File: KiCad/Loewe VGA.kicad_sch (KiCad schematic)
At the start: 29 parts, among them U1 74HCT86

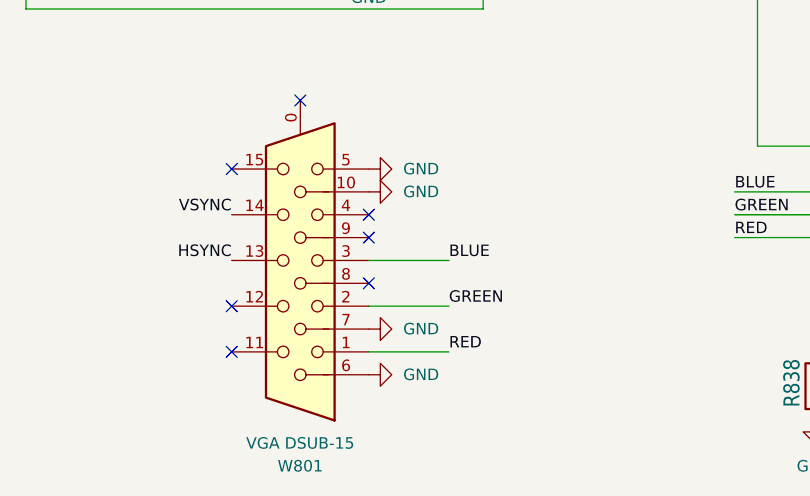
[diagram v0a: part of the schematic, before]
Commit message: Connect VGA pin 8 to GND.
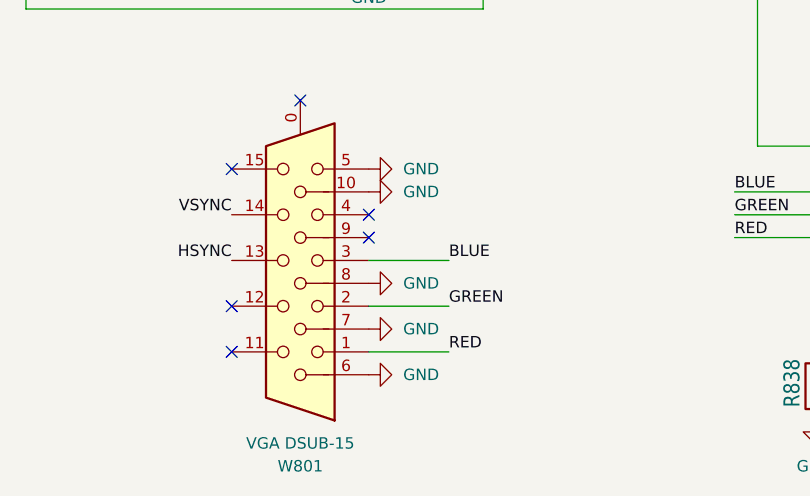
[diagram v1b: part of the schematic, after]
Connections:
- net GND: now also W801.8
- no-connect marks 7 -> 6
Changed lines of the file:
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@@
 		(at 132.08 143.51)
 	)
-	(no_connect
-		(at 132.08 151.13)
-	)
 	(wire
 		(pts
@@
 					(unit 1)
 				)
+			)
+		)
+	)
+	(symbol
+		(lib_id "power:GND")
+		(at 132.08 151.13 90)
+		(unit 1)
+		(exclude_from_sim no)
+		(in_bom yes)
+		(on_board yes)
+		(dnp no)
+		(fields_autoplaced yes)
+		(property "Reference" "#PWR013"
+			(at 138.43 151.13 0)
+			(effects
+				(font
+					(size 1.27 1.27)
+				)
+				(hide yes)
+			)
+		)
+		(property "Value" "GND"
+			(at 135.89 151.1301 90)
+			(effects
+				(font
+					(size 1.27 1.27)
+				)
+				(justify right)
+			)
+		)
+		(property "Footprint" ""
+			(at 132.08 151.13 0)
+			(effects
+				(font
+					(size 1.27 1.27)
+				)
+				(hide yes)
+			)
+		)
+		(property "Datasheet" ""
+			(at 132.08 151.13 0)
+			(effects
+				(font
+					(size 1.27 1.27)
+				)
+				(hide yes)
+			)
+		)
+		(property "Description" "Power symbol creates a global label with name \"GND\" , ground"
+			(at 132.08 151.13 0)
+			(effects
+				(font
+					(size 1.27 1.27)
+				)
+				(hide yes)
+			)
+		)
+		(pin "1"
+		)
+		(instances
+			(project "Loewe VGA"
+				(path "/a1c137e0-772e-4d1d-9f66-964ee6eebaf2"
+					(reference "#PWR013")
+					(unit 1)
+				)

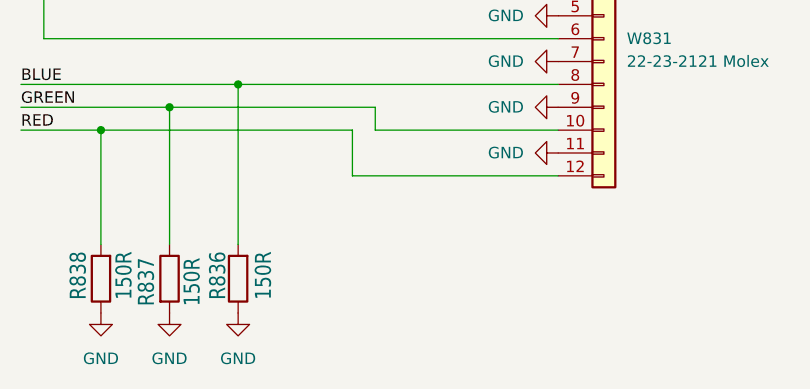
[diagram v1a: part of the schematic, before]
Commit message: Do not solder R836~R838 RGB input termination resistors for Q2400 chassis. Source: Loewe Q2400 service manual, p.2-22.
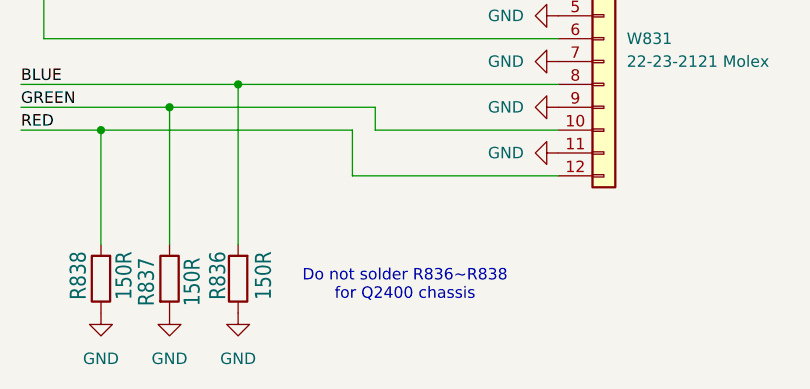
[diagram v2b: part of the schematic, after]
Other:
- note added: "Do not solder R836~R838 for Q2400 chassis"
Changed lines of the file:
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@@
+		)
+	)
+	(text "Do not solder R836~R838\nfor Q2400 chassis"
+		(exclude_from_sim no)
+		(at 215.392 163.322 0)
+		(effects
+			(font
+				(size 1.27 1.27)
+			)
 		)
 	)

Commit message: Replace custom 3225 footprint for L826, L816 with standard 1210(3225). Add 4.7uH value for L826, L816 to schematic (use value from Q2300 board).
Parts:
- L816, L826: value LL3225M -> 4u7; footprint Loewe VGA:L3225M -> Inductor_SMD:L_1210_3225Metric_Pad1.42x2.65mm_HandSolder
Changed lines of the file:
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@@
 			)
 		)
-		(property "Value" "LL3225M"
+		(property "Value" "4u7"
 			(at 88.9 52.832 90)
 			(effects
@@
 			)
 		)
-		(property "Footprint" "Loewe VGA:L3225M"
+		(property "Footprint" "Inductor_SMD:L_1210_3225Metric_Pad1.42x2.65mm_HandSolder"
 			(at 92.71 49.53 0)
 			(effects
@@
 			)
 		)
-		(property "Value" "LL3225M"
+		(property "Value" "4u7"
 			(at 83.82 90.932 90)
 			(effects
@@
 			)
 		)
-		(property "Footprint" "Loewe VGA:L3225M"
+		(property "Footprint" "Inductor_SMD:L_1210_3225Metric_Pad1.42x2.65mm_HandSolder"
 			(at 87.63 87.63 0)
 			(effects

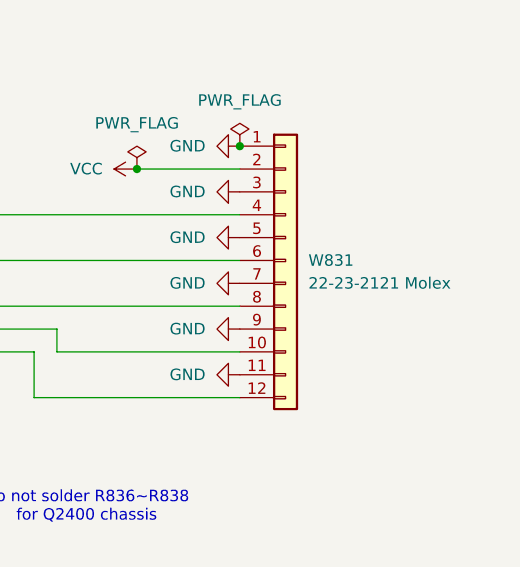
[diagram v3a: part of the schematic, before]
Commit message: Replace JST XH 2.50 mm with custom 2.54 mm. Remove unused Molex 22-23-2121 footprint. Add version V.1.1 label to PCB silkscreen.
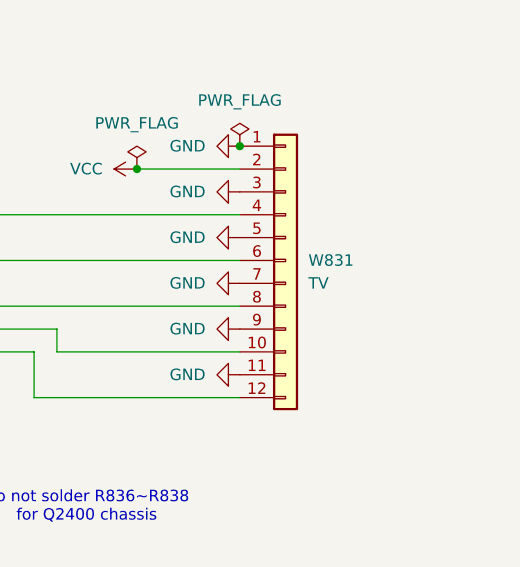
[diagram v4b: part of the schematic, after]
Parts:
- W831: value 22-23-2121 Molex -> TV; footprint Loewe VGA:22-23-2121 -> JST_XH_S10B_2.54mm:JST_XH_B12B-XH-A_1x12_P2.54mm_Vertical
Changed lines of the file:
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@@
 			)
 		)
-		(property "Value" "22-23-2121 Molex"
+		(property "Value" "TV"
 			(at 240.03 138.4299 0)
 			(effects
@@
 			)
 		)
-		(property "Footprint" "Loewe VGA:22-23-2121"
+		(property "Footprint" "JST_XH_S10B_2.54mm:JST_XH_B12B-XH-A_1x12_P2.54mm_Vertical"
 			(at 237.49 135.89 0)
 			(effects

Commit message: Replace incorrect Connector_Dsub:DSUB-15-HD_Male with short Connector_Dsub:DSUB-15-HD_Female. Move VGA and TV connectors to back side. Reduce PCB width. Change VCC tracks width from 0.3 to 0.5 mm. Align board info text.
PCB version updated to 1.2.
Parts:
- W801: footprint Connector_Dsub:DSUB-15-HD_Male_Horizontal_P2.29x1.98mm_EdgePinOffset8.35mm_Housed_MountingHolesOffset10.89mm -> Connector_Dsub:DSUB-15-HD_Female_Horizontal_P2.29x1.98mm_EdgePinOffset3.03mm_Housed_MountingHolesOffset4.94mm
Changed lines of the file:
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@@
 			)
 		)
-		(property "Footprint" "Connector_Dsub:DSUB-15-HD_Male_Horizontal_P2.29x1.98mm_EdgePinOffset8.35mm_Housed_MountingHolesOffset10.89mm"
+		(property "Footprint" "Connector_Dsub:DSUB-15-HD_Female_Horizontal_P2.29x1.98mm_EdgePinOffset3.03mm_Housed_MountingHolesOffset4.94mm"
 			(at 148.59 158.75 0)
 			(effects

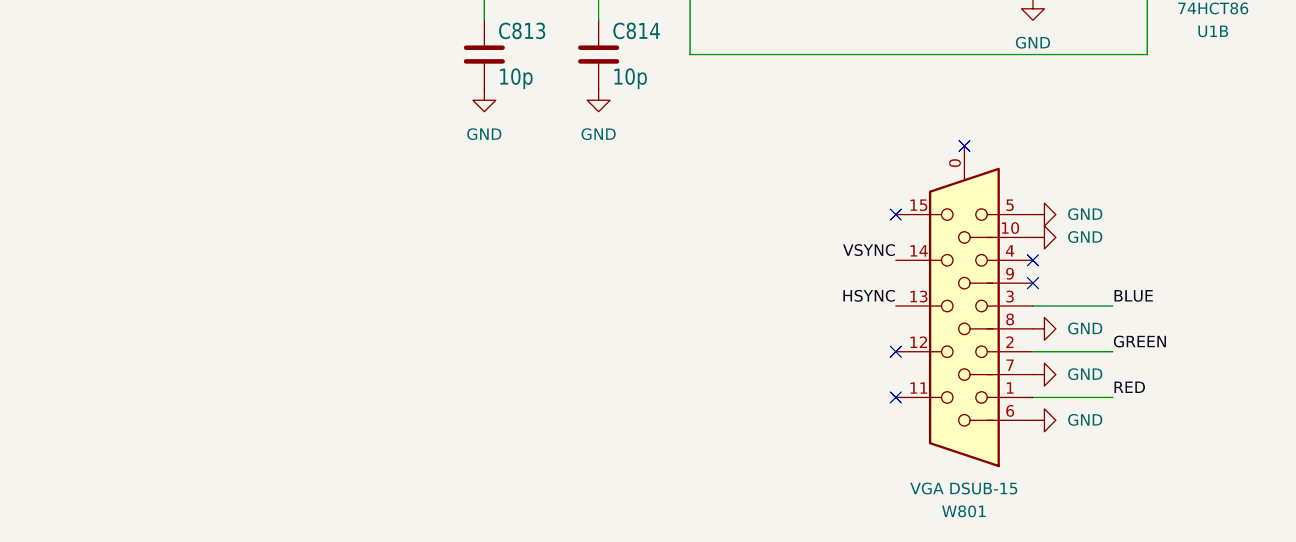
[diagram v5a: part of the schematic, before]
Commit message: Add EDID EEPROM option for 848x480@60Hz mode auto detection with widescreen TVs.
PCB version 1.2.
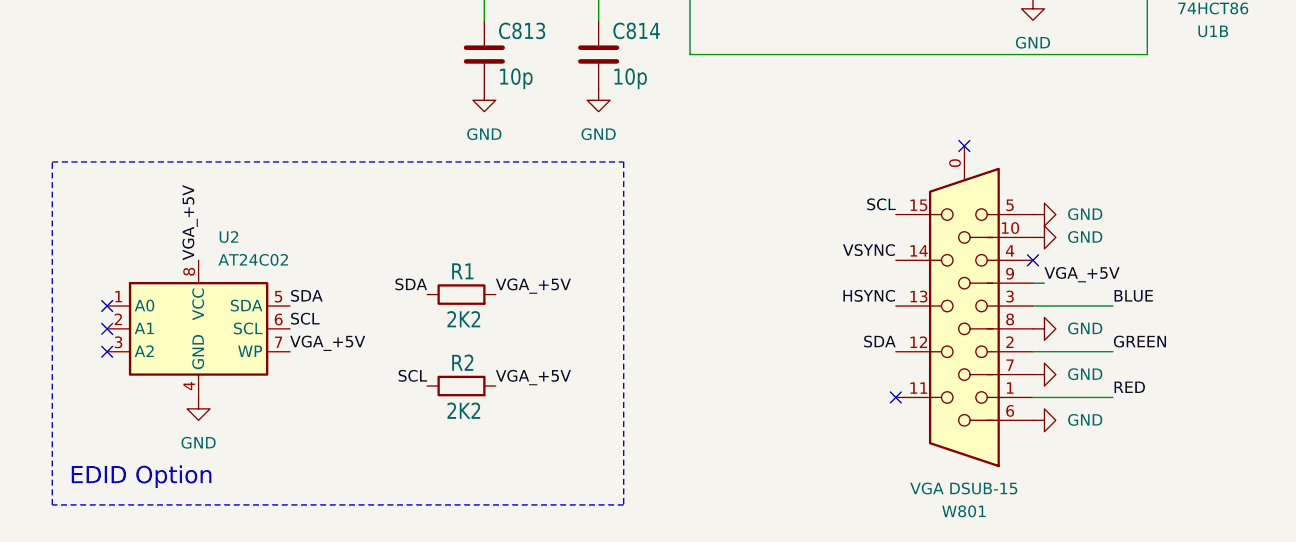
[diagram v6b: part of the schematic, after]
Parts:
- added R1, R2: 2K2, Resistor_SMD:R_0805_2012Metric_Pad1.20x1.40mm_HandSolder, symbol Device:R
- added U2: AT24C02, Package_SO:SOIC-8_3.9x4.9mm_P1.27mm, symbol Memory_EEPROM:AT24CS02-SSHM
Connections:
- net GND: now also U2.4 (GND)
- net SDA: now reaches W801.12
- net SDA: now also R1.1, U2.5 (SDA)
- net SCL: now reaches W801.15
- net SCL: now also R2.1, U2.6 (SCL)
- net VGA_+5V: now reaches W801.9
- net VGA_+5V: now also R1.2, R2.2, U2.7 (WP), U2.8 (VCC)
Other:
- note added: "EDID Option"
